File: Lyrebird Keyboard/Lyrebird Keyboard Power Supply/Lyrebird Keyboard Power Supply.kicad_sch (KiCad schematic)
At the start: 22 parts, among them IC1 L7915CV, IC2 L78S15CV, J10 +15V, J10 +VED, J10 +VT, J10 -15V, J10 30V, J10 AC IN 2, J9 AC IN 1, U1 DF06S

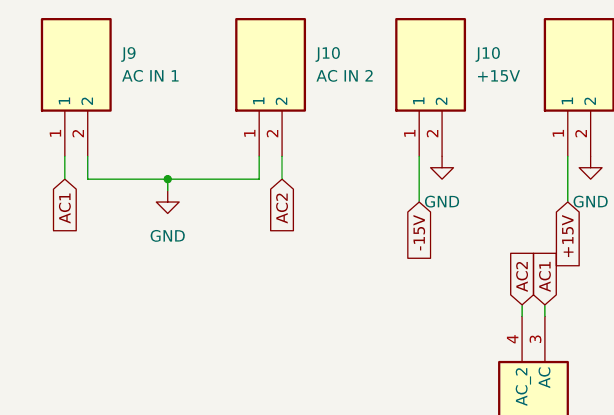
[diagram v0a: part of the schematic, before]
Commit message: Added KiCAD library
Uploaded current ECAD library, to facilitate editing away from main work computer
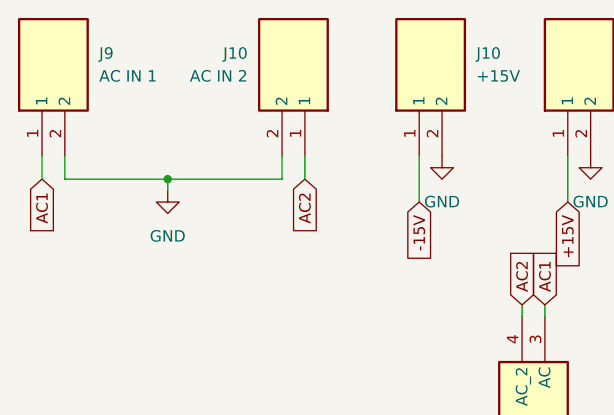
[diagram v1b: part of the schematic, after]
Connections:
- net AC2: now also J10.1; no longer J10.2
- net GND: now also J10.2; no longer J10.1
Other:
- moved on the sheet: J10, J9
